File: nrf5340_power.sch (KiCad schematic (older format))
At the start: 0 parts

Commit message: first rev pcb without impedance matching
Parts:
- added C29, C30: 10uF, Capacitor_SMD:C_0201_0603Metric, symbol Device:C_Small
- added D1: LED, LED_SMD:LED_0402_1005Metric, symbol Device:LED
- added D2: MBR120, Diode_SMD:D_SOD-123, symbol Device:D_Zener_Small
- added Q1: Q_PMOS_GSD, Package_TO_SOT_SMD:SOT-23, symbol Device:Q_PMOS_GSD
- added R4, R6: 100k, Resistor_SMD:R_0201_0603Metric, symbol Device:R_Small
- added R5: 68R, Resistor_SMD:R_0201_0603Metric, symbol Device:R_Small
- added U2: AP2112K-3.3, Package_TO_SOT_SMD:SOT-23-5, symbol Regulator_Linear:AP2112K-3.3
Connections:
- new net: C29.1, D2.1 (K), Q1.2 (S), R6.1, U2.1 (VIN)
- new net: R6.2, U2.3 (EN)
- new net: D1.2 (A), R5.2
- new net GND: C29.2, C30.2, D1.1 (K), R4.2, U2.2 (GND)
- new net VBAT: Q1.3 (D)
- new net VBUS: D2.2 (A), Q1.1 (G), R4.1
- new net VDD_nRF: C30.1, R5.1, U2.5 (VOUT)
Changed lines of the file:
@@
 EESchema Schematic File Version 4
-LIBS:nrf5340_module-cache
 EELAYER 30 0
 EELAYER END
 $Descr A4 11693 8268
 encoding utf-8
-Sheet 1 3
+Sheet 3 3
 Title ""
 Date ""
@@
 Comment4 ""
 $EndDescr
+$Comp
+L Device:Q_PMOS_GSD Q1
+U 1 1 5E164004
+P 1450 1050
+F 0 "Q1" H 1655 1096 50  0000 L CNN
+F 1 "Q_PMOS_GSD" H 1655 1005 50  0000 L CNN
+F 2 "Package_TO_SOT_SMD:SOT-23" H 1650 1150 50  0001 C CNN
+F 3 "~" H 1450 1050 50  0001 C CNN
+	1    1450 1050
+	1    0    0    -1
+$EndComp
+$Comp
+L Device:R_Small R4
+U 1 1 5E1648ED
+P 1000 1550
+F 0 "R4" H 750 1600 50  0000 L CNN
+F 1 "100k" H 750 1500 50  0000 L CNN
+F 2 "Resistor_SMD:R_0201_0603Metric" H 1000 1550 50  0001 C CNN
+F 3 "~" H 1000 1550 50  0001 C CNN
+	1    1000 1550
+	1    0    0    -1
+$EndComp
+$Comp
+L Device:D_Zener_Small D2
+U 1 1 5E165282
+P 1300 1400
+F 0 "D2" H 1300 1195 50  0000 C CNN
+F 1 "MBR120" H 1300 1286 50  0000 C CNN
+F 2 "Diode_SMD:D_SOD-123" V 1300 1400 50  0001 C CNN
+F 3 "~" V 1300 1400 50  0001 C CNN
+	1    1300 1400
+	-1   0    0    1
+$EndComp
+$Comp
+L Device:C_Small C29
+U 1 1 5E165C53
+P 1550 1550
+F 0 "C29" H 1642 1596 50  0000 L CNN
+F 1 "10uF" H 1642 1505 50  0000 L CNN
+F 2 "Capacitor_SMD:C_0201_0603Metric" H 1550 1550 50  0001 C CNN
+F 3 "~" H 1550 1550 50  0001 C CNN
+	1    1550 1550
+	1    0    0    -1
+$EndComp
+$Comp
+L Device:C_Small C30
+U 1 1 5E16615D
+P 2800 1550
+F 0 "C30" H 2892 1596 50  0000 L CNN
+F 1 "10uF" H 2892 1505 50  0000 L CNN
+F 2 "Capacitor_SMD:C_0201_0603Metric" H 2800 1550 50  0001 C CNN
+F 3 "~" H 2800 1550 50  0001 C CNN
+	1    2800 1550
+	1    0    0    -1
+$EndComp
+$Comp
+L Device:R_Small R6
+U 1 1 5E1662E7
+P 2000 1500
+F 0 "R6" V 2100 1500 50  0000 C CNN
+F 1 "100k" V 2200 1500 50  0000 C CNN
+F 2 "Resistor_SMD:R_0201_0603Metric" H 2000 1500 50  0001 C CNN
+F 3 "~" H 2000 1500 50  0001 C CNN
+	1    2000 1500
+	0    -1   1    0
+$EndComp
+$Comp
+L Regulator_Linear:AP2112K-3.3 U2
+U 1 1 5E166BA6
+P 2450 1500
+F 0 "U2" H 2450 1842 50  0000 C CNN
+F 1 "AP2112K-3.3" H 2450 1751 50  0000 C CNN
+F 2 "Package_TO_SOT_SMD:SOT-23-5" H 2450 1825 50  0001 C CNN
+F 3 "https://www.diodes.com/assets/Datasheets/AP2112.pdf" H 2450 1600 50  0001 C CNN
+	1    2450 1500
+	1    0    0    -1
+$EndComp
+Text GLabel 2850 1400 2    50   Input ~ 0
+VDD_nRF
+Text GLabel 1000 800  2    50   Input ~ 0
+VBUS
+Text GLabel 1550 800  2    50   Input ~ 0
+VBAT
+Wire Wire Line
+	1550 800  1550 850
+Wire Wire Line
+	1550 1400 1400 1400
+Wire Wire Line
+	1550 1250 1550 1400
+Wire Wire Line
+	1200 1400 1000 1400
+Wire Wire Line
+	1000 1450 1000 1400
+Connection ~ 1000 1400
+Wire Wire Line
+	1000 800  1000 1050
+Wire Wire Line
+	1250 1050 1000 1050
+Connection ~ 1000 1050
+Wire Wire Line
+	1000 1050 1000 1400
+Wire Wire Line
+	1550 1450 1550 1400
+Connection ~ 1550 1400
+Wire Wire Line
+	2100 1500 2150 1500
+Wire Wire Line
+	2150 1400 1850 1400
+Wire Wire Line
+	1850 1400 1850 1500
+Wire Wire Line
+	1850 1500 1900 1500
+Connection ~ 1850 1400
+$Comp
+L power:GND #PWR013
+U 1 1 5E177C45
+P 2800 1700
+F 0 "#PWR013" H 2800 1450 50  0001 C CNN
+F 1 "GND" H 2805 1527 50  0000 C CNN
+F 2 "" H 2800 1700 50  0001 C CNN
+F 3 "" H 2800 1700 50  0001 C CNN
+	1    2800 1700
+	1    0    0    -1
+$EndComp
+$Comp
+L power:GND #PWR012
+U 1 1 5E177E44
+P 2450 1850
+F 0 "#PWR012" H 2450 1600 50  0001 C CNN
+F 1 "GND" H 2455 1677 50  0000 C CNN
+F 2 "" H 2450 1850 50  0001 C CNN
+F 3 "" H 2450 1850 50  0001 C CNN
+	1    2450 1850
+	1    0    0    -1
+$EndComp
+$Comp
+L power:GND #PWR011
+U 1 1 5E17842E
+P 1550 1700
+F 0 "#PWR011" H 1550 1450 50  0001 C CNN
+F 1 "GND" H 1555 1527 50  0000 C CNN
+F 2 "" H 1550 1700 50  0001 C CNN
+F 3 "" H 1550 1700 50  0001 C CNN
+	1    1550 1700
+	1    0    0    -1
+$EndComp
+$Comp
+L power:GND #PWR09
+U 1 1 5E178752
+P 1000 1700
+F 0 "#PWR09" H 1000 1450 50  0001 C CNN
+F 1 "GND" H 1005 1527 50  0000 C CNN
+F 2 "" H 1000 1700 50  0001 C CNN
+F 3 "" H 1000 1700 50  0001 C CNN
+	1    1000 1700
+	1    0    0    -1
+$EndComp
+Wire Wire Line
+	1550 1400 1850 1400
+Wire Wire Line
+	1550 1650 1550 1700
+Wire Wire Line
+	1000 1650 1000 1700
+Wire Wire Line
+	2450 1800 2450 1850
+Wire Wire Line
+	2800 1650 2800 1700
+Wire Wire Line
+	2850 1400 2800 1400
+Wire Wire Line
+	2800 1400 2800 1450
+Connection ~ 2800 1400
+Wire Wire Line
+	2800 1400 2750 1400
+$Comp
+L Device:LED D1
+U 1 1 5E1852C7
+P 1000 2850
+F 0 "D1" V 1039 2733 50  0000 R CNN
+F 1 "LED" V 948 2733 50  0000 R CNN
+F 2 "LED_SMD:LED_0402_1005Metric" H 1000 2850 50  0001 C CNN
+F 3 "~" H 1000 2850 50  0001 C CNN
+	1    1000 2850
+	0    -1   -1   0
+$EndComp
+Text GLabel 1000 2350 2    50   Input ~ 0
+VDD_nRF
+$Comp
+L Device:R_Small R5
+U 1 1 5E18637C
+P 1000 2550
+F 0 "R5" H 850 2600 50  0000 L CNN
+F 1 "68R" H 800 2500 50  0000 L CNN
+F 2 "Resistor_SMD:R_0201_0603Metric" H 1000 2550 50  0001 C CNN
+F 3 "~" H 1000 2550 50  0001 C CNN
+	1    1000 2550
+	1    0    0    -1
+$EndComp
+Wire Wire Line
+	1000 2350 1000 2450
+Wire Wire Line
+	1000 2650 1000 2700
+Wire Wire Line
+	1000 3000 1000 3050
+$Comp
+L power:GND #PWR010
+U 1 1 5E187B31
+P 1000 3050
+F 0 "#PWR010" H 1000 2800 50  0001 C CNN
+F 1 "GND" H 1005 2877 50  0000 C CNN
+F 2 "" H 1000 3050 50  0001 C CNN
+F 3 "" H 1000 3050 50  0001 C CNN
+	1    1000 3050
+	1    0    0    -1
+$EndComp
 $EndSCHEMATC

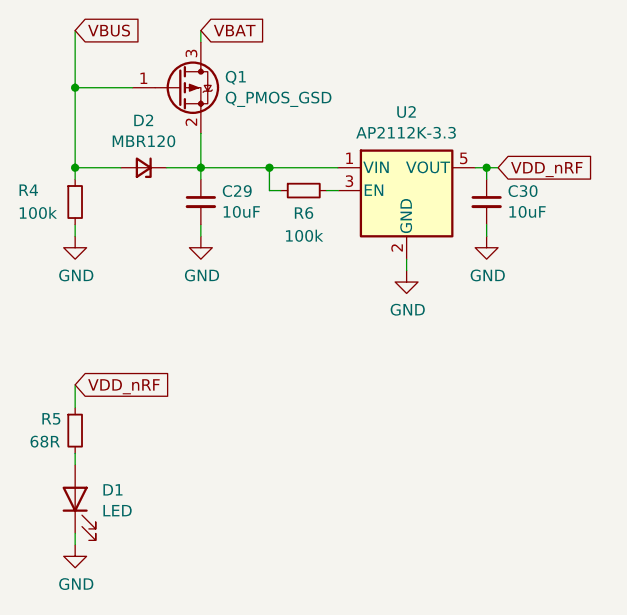
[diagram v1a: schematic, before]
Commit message: fix traces underneath nrf gnd pad and VDD_HV
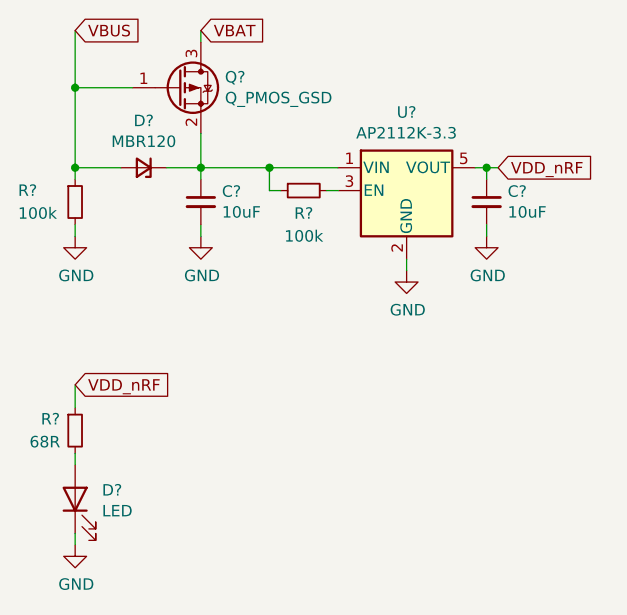
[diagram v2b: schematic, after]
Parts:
- renumbered C29 to C?, C30 to C?, D2 to D?, D1 to D?, Q1 to Q?, R4 to R?, R6 to R?, R5 to R?, U2 to U?
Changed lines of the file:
@@
 EESchema Schematic File Version 4
+LIBS:nrf5340_module-cache
 EELAYER 30 0
 EELAYER END
@@
 $EndDescr
 $Comp
-L Device:Q_PMOS_GSD Q1
+L Device:Q_PMOS_GSD Q?
 U 1 1 5E164004
 P 1450 1050
-F 0 "Q1" H 1655 1096 50  0000 L CNN
+F 0 "Q?" H 1655 1096 50  0000 L CNN
 F 1 "Q_PMOS_GSD" H 1655 1005 50  0000 L CNN
 F 2 "Package_TO_SOT_SMD:SOT-23" H 1650 1150 50  0001 C CNN
@@
 $EndComp
 $Comp
-L Device:R_Small R4
+L Device:R_Small R?
 U 1 1 5E1648ED
 P 1000 1550
-F 0 "R4" H 750 1600 50  0000 L CNN
+F 0 "R?" H 750 1600 50  0000 L CNN
 F 1 "100k" H 750 1500 50  0000 L CNN
 F 2 "Resistor_SMD:R_0201_0603Metric" H 1000 1550 50  0001 C CNN
@@
 $EndComp
 $Comp
-L Device:D_Zener_Small D2
+L Device:D_Zener_Small D?
 U 1 1 5E165282
 P 1300 1400
-F 0 "D2" H 1300 1195 50  0000 C CNN
+F 0 "D?" H 1300 1195 50  0000 C CNN
 F 1 "MBR120" H 1300 1286 50  0000 C CNN
 F 2 "Diode_SMD:D_SOD-123" V 1300 1400 50  0001 C CNN
@@
 $EndComp
 $Comp
-L Device:C_Small C29
+L Device:C_Small C?
 U 1 1 5E165C53
 P 1550 1550
-F 0 "C29" H 1642 1596 50  0000 L CNN
+F 0 "C?" H 1642 1596 50  0000 L CNN
 F 1 "10uF" H 1642 1505 50  0000 L CNN
 F 2 "Capacitor_SMD:C_0201_0603Metric" H 1550 1550 50  0001 C CNN
@@
 $EndComp
 $Comp
-L Device:C_Small C30
+L Device:C_Small C?
 U 1 1 5E16615D
 P 2800 1550
-F 0 "C30" H 2892 1596 50  0000 L CNN
+F 0 "C?" H 2892 1596 50  0000 L CNN
 F 1 "10uF" H 2892 1505 50  0000 L CNN
 F 2 "Capacitor_SMD:C_0201_0603Metric" H 2800 1550 50  0001 C CNN
@@
 $EndComp
 $Comp
-L Device:R_Small R6
+L Device:R_Small R?
 U 1 1 5E1662E7
 P 2000 1500
-F 0 "R6" V 2100 1500 50  0000 C CNN
+F 0 "R?" V 2100 1500 50  0000 C CNN
 F 1 "100k" V 2200 1500 50  0000 C CNN
 F 2 "Resistor_SMD:R_0201_0603Metric" H 2000 1500 50  0001 C CNN
@@
 $EndComp
 $Comp
-L Regulator_Linear:AP2112K-3.3 U2
+L Regulator_Linear:AP2112K-3.3 U?
 U 1 1 5E166BA6
 P 2450 1500
-F 0 "U2" H 2450 1842 50  0000 C CNN
+F 0 "U?" H 2450 1842 50  0000 C CNN
 F 1 "AP2112K-3.3" H 2450 1751 50  0000 C CNN
 F 2 "Package_TO_SOT_SMD:SOT-23-5" H 2450 1825 50  0001 C CNN
@@
 Connection ~ 1850 1400
 $Comp
-L power:GND #PWR013
+L power:GND #PWR?
 U 1 1 5E177C45
 P 2800 1700
-F 0 "#PWR013" H 2800 1450 50  0001 C CNN
+F 0 "#PWR?" H 2800 1450 50  0001 C CNN
 F 1 "GND" H 2805 1527 50  0000 C CNN
 F 2 "" H 2800 1700 50  0001 C CNN
@@
 $EndComp
 $Comp
-L power:GND #PWR012
+L power:GND #PWR?
 U 1 1 5E177E44
 P 2450 1850
-F 0 "#PWR012" H 2450 1600 50  0001 C CNN
+F 0 "#PWR?" H 2450 1600 50  0001 C CNN
 F 1 "GND" H 2455 1677 50  0000 C CNN
 F 2 "" H 2450 1850 50  0001 C CNN
@@
 $EndComp
 $Comp
-L power:GND #PWR011
+L power:GND #PWR?
 U 1 1 5E17842E
 P 1550 1700
-F 0 "#PWR011" H 1550 1450 50  0001 C CNN
+F 0 "#PWR?" H 1550 1450 50  0001 C CNN
 F 1 "GND" H 1555 1527 50  0000 C CNN
 F 2 "" H 1550 1700 50  0001 C CNN
@@
 $EndComp
 $Comp
-L power:GND #PWR09
+L power:GND #PWR?
 U 1 1 5E178752
 P 1000 1700
-F 0 "#PWR09" H 1000 1450 50  0001 C CNN
+F 0 "#PWR?" H 1000 1450 50  0001 C CNN
 F 1 "GND" H 1005 1527 50  0000 C CNN
 F 2 "" H 1000 1700 50  0001 C CNN
@@
 	2800 1400 2750 1400
 $Comp
-L Device:LED D1
+L Device:LED D?
 U 1 1 5E1852C7
 P 1000 2850
-F 0 "D1" V 1039 2733 50  0000 R CNN
+F 0 "D?" V 1039 2733 50  0000 R CNN
 F 1 "LED" V 948 2733 50  0000 R CNN
 F 2 "LED_SMD:LED_0402_1005Metric" H 1000 2850 50  0001 C CNN
@@
 VDD_nRF
 $Comp
-L Device:R_Small R5
+L Device:R_Small R?
 U 1 1 5E18637C
 P 1000 2550
-F 0 "R5" H 850 2600 50  0000 L CNN
+F 0 "R?" H 850 2600 50  0000 L CNN
 F 1 "68R" H 800 2500 50  0000 L CNN
 F 2 "Resistor_SMD:R_0201_0603Metric" H 1000 2550 50  0001 C CNN
@@
 	1000 3000 1000 3050
 $Comp
-L power:GND #PWR010
+L power:GND #PWR?
 U 1 1 5E187B31
 P 1000 3050
-F 0 "#PWR010" H 1000 2800 50  0001 C CNN
+F 0 "#PWR?" H 1000 2800 50  0001 C CNN
 F 1 "GND" H 1005 2877 50  0000 C CNN
 F 2 "" H 1000 3050 50  0001 C CNN

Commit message: fix vdd_hv
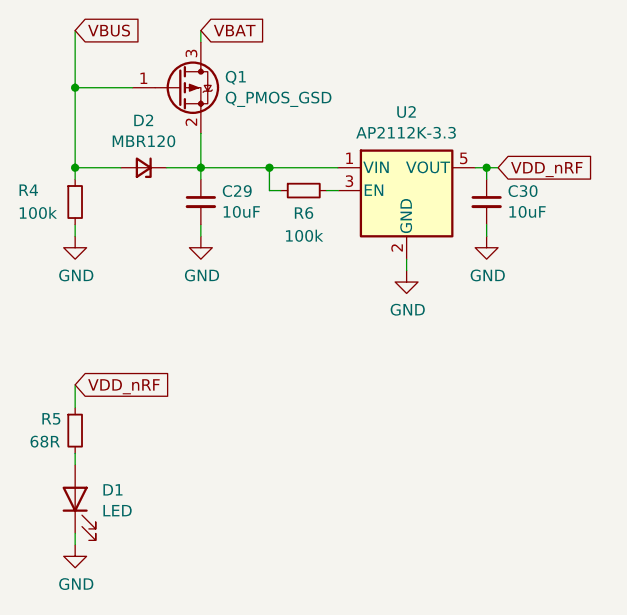
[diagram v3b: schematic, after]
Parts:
- gave numbers to parts that had none: 9
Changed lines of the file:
@@
 $EndDescr
 $Comp
-L Device:Q_PMOS_GSD Q?
+L Device:Q_PMOS_GSD Q1
 U 1 1 5E164004
 P 1450 1050
-F 0 "Q?" H 1655 1096 50  0000 L CNN
+F 0 "Q1" H 1655 1096 50  0000 L CNN
 F 1 "Q_PMOS_GSD" H 1655 1005 50  0000 L CNN
 F 2 "Package_TO_SOT_SMD:SOT-23" H 1650 1150 50  0001 C CNN
@@
 $EndComp
 $Comp
-L Device:R_Small R?
+L Device:R_Small R4
 U 1 1 5E1648ED
 P 1000 1550
-F 0 "R?" H 750 1600 50  0000 L CNN
+F 0 "R4" H 750 1600 50  0000 L CNN
 F 1 "100k" H 750 1500 50  0000 L CNN
 F 2 "Resistor_SMD:R_0201_0603Metric" H 1000 1550 50  0001 C CNN
@@
 $EndComp
 $Comp
-L Device:D_Zener_Small D?
+L Device:D_Zener_Small D2
 U 1 1 5E165282
 P 1300 1400
-F 0 "D?" H 1300 1195 50  0000 C CNN
+F 0 "D2" H 1300 1195 50  0000 C CNN
 F 1 "MBR120" H 1300 1286 50  0000 C CNN
 F 2 "Diode_SMD:D_SOD-123" V 1300 1400 50  0001 C CNN
@@
 $EndComp
 $Comp
-L Device:C_Small C?
+L Device:C_Small C29
 U 1 1 5E165C53
 P 1550 1550
-F 0 "C?" H 1642 1596 50  0000 L CNN
+F 0 "C29" H 1642 1596 50  0000 L CNN
 F 1 "10uF" H 1642 1505 50  0000 L CNN
 F 2 "Capacitor_SMD:C_0201_0603Metric" H 1550 1550 50  0001 C CNN
@@
 $EndComp
 $Comp
-L Device:C_Small C?
+L Device:C_Small C30
 U 1 1 5E16615D
 P 2800 1550
-F 0 "C?" H 2892 1596 50  0000 L CNN
+F 0 "C30" H 2892 1596 50  0000 L CNN
 F 1 "10uF" H 2892 1505 50  0000 L CNN
 F 2 "Capacitor_SMD:C_0201_0603Metric" H 2800 1550 50  0001 C CNN
@@
 $EndComp
 $Comp
-L Device:R_Small R?
+L Device:R_Small R6
 U 1 1 5E1662E7
 P 2000 1500
-F 0 "R?" V 2100 1500 50  0000 C CNN
+F 0 "R6" V 2100 1500 50  0000 C CNN
 F 1 "100k" V 2200 1500 50  0000 C CNN
 F 2 "Resistor_SMD:R_0201_0603Metric" H 2000 1500 50  0001 C CNN
@@
 $EndComp
 $Comp
-L Regulator_Linear:AP2112K-3.3 U?
+L Regulator_Linear:AP2112K-3.3 U2
 U 1 1 5E166BA6
 P 2450 1500
-F 0 "U?" H 2450 1842 50  0000 C CNN
+F 0 "U2" H 2450 1842 50  0000 C CNN
 F 1 "AP2112K-3.3" H 2450 1751 50  0000 C CNN
 F 2 "Package_TO_SOT_SMD:SOT-23-5" H 2450 1825 50  0001 C CNN
@@
 Connection ~ 1850 1400
 $Comp
-L power:GND #PWR?
+L power:GND #PWR0130
 U 1 1 5E177C45
 P 2800 1700
-F 0 "#PWR?" H 2800 1450 50  0001 C CNN
+F 0 "#PWR0130" H 2800 1450 50  0001 C CNN
 F 1 "GND" H 2805 1527 50  0000 C CNN
 F 2 "" H 2800 1700 50  0001 C CNN
@@
 $EndComp
 $Comp
-L power:GND #PWR?
+L power:GND #PWR0131
 U 1 1 5E177E44
 P 2450 1850
-F 0 "#PWR?" H 2450 1600 50  0001 C CNN
+F 0 "#PWR0131" H 2450 1600 50  0001 C CNN
 F 1 "GND" H 2455 1677 50  0000 C CNN
 F 2 "" H 2450 1850 50  0001 C CNN
@@
 $EndComp
 $Comp
-L power:GND #PWR?
+L power:GND #PWR0132
 U 1 1 5E17842E
 P 1550 1700
-F 0 "#PWR?" H 1550 1450 50  0001 C CNN
+F 0 "#PWR0132" H 1550 1450 50  0001 C CNN
 F 1 "GND" H 1555 1527 50  0000 C CNN
 F 2 "" H 1550 1700 50  0001 C CNN
@@
 $EndComp
 $Comp
-L power:GND #PWR?
+L power:GND #PWR0133
 U 1 1 5E178752
 P 1000 1700
-F 0 "#PWR?" H 1000 1450 50  0001 C CNN
+F 0 "#PWR0133" H 1000 1450 50  0001 C CNN
 F 1 "GND" H 1005 1527 50  0000 C CNN
 F 2 "" H 1000 1700 50  0001 C CNN
@@
 	2800 1400 2750 1400
 $Comp
-L Device:LED D?
+L Device:LED D1
 U 1 1 5E1852C7
 P 1000 2850
-F 0 "D?" V 1039 2733 50  0000 R CNN
+F 0 "D1" V 1039 2733 50  0000 R CNN
 F 1 "LED" V 948 2733 50  0000 R CNN
 F 2 "LED_SMD:LED_0402_1005Metric" H 1000 2850 50  0001 C CNN
@@
 VDD_nRF
 $Comp
-L Device:R_Small R?
+L Device:R_Small R5
 U 1 1 5E18637C
 P 1000 2550
-F 0 "R?" H 850 2600 50  0000 L CNN
+F 0 "R5" H 850 2600 50  0000 L CNN
 F 1 "68R" H 800 2500 50  0000 L CNN
 F 2 "Resistor_SMD:R_0201_0603Metric" H 1000 2550 50  0001 C CNN
@@
 	1000 3000 1000 3050
 $Comp
-L power:GND #PWR?
+L power:GND #PWR0134
 U 1 1 5E187B31
 P 1000 3050
-F 0 "#PWR?" H 1000 2800 50  0001 C CNN
+F 0 "#PWR0134" H 1000 2800 50  0001 C CNN
 F 1 "GND" H 1005 2877 50  0000 C CNN
 F 2 "" H 1000 3050 50  0001 C CNN

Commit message: fix vddh stuff
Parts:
- renumbered C29 to C?, C30 to C?, D2 to D?, D1 to D?, Q1 to Q?, R4 to R?, R6 to R?, R5 to R?, U2 to U?
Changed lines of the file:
@@
 $Descr A4 11693 8268
 encoding utf-8
-Sheet 3 3
+Sheet 3 7
 Title ""
 Date ""
@@
 $EndDescr
 $Comp
-L Device:Q_PMOS_GSD Q1
+L Device:Q_PMOS_GSD Q?
 U 1 1 5E164004
 P 1450 1050
-F 0 "Q1" H 1655 1096 50  0000 L CNN
+F 0 "Q?" H 1655 1096 50  0000 L CNN
 F 1 "Q_PMOS_GSD" H 1655 1005 50  0000 L CNN
 F 2 "Package_TO_SOT_SMD:SOT-23" H 1650 1150 50  0001 C CNN
@@
 $EndComp
 $Comp
-L Device:R_Small R4
+L Device:R_Small R?
 U 1 1 5E1648ED
 P 1000 1550
-F 0 "R4" H 750 1600 50  0000 L CNN
+F 0 "R?" H 750 1600 50  0000 L CNN
 F 1 "100k" H 750 1500 50  0000 L CNN
 F 2 "Resistor_SMD:R_0201_0603Metric" H 1000 1550 50  0001 C CNN
@@
 $EndComp
 $Comp
-L Device:D_Zener_Small D2
+L Device:D_Zener_Small D?
 U 1 1 5E165282
 P 1300 1400
-F 0 "D2" H 1300 1195 50  0000 C CNN
+F 0 "D?" H 1300 1195 50  0000 C CNN
 F 1 "MBR120" H 1300 1286 50  0000 C CNN
 F 2 "Diode_SMD:D_SOD-123" V 1300 1400 50  0001 C CNN
@@
 $EndComp
 $Comp
-L Device:C_Small C29
+L Device:C_Small C?
 U 1 1 5E165C53
 P 1550 1550
-F 0 "C29" H 1642 1596 50  0000 L CNN
+F 0 "C?" H 1642 1596 50  0000 L CNN
 F 1 "10uF" H 1642 1505 50  0000 L CNN
 F 2 "Capacitor_SMD:C_0201_0603Metric" H 1550 1550 50  0001 C CNN
@@
 $EndComp
 $Comp
-L Device:C_Small C30
+L Device:C_Small C?
 U 1 1 5E16615D
 P 2800 1550
-F 0 "C30" H 2892 1596 50  0000 L CNN
+F 0 "C?" H 2892 1596 50  0000 L CNN
 F 1 "10uF" H 2892 1505 50  0000 L CNN
 F 2 "Capacitor_SMD:C_0201_0603Metric" H 2800 1550 50  0001 C CNN
@@
 $EndComp
 $Comp
-L Device:R_Small R6
+L Device:R_Small R?
 U 1 1 5E1662E7
 P 2000 1500
-F 0 "R6" V 2100 1500 50  0000 C CNN
+F 0 "R?" V 2100 1500 50  0000 C CNN
 F 1 "100k" V 2200 1500 50  0000 C CNN
 F 2 "Resistor_SMD:R_0201_0603Metric" H 2000 1500 50  0001 C CNN
@@
 $EndComp
 $Comp
-L Regulator_Linear:AP2112K-3.3 U2
+L Regulator_Linear:AP2112K-3.3 U?
 U 1 1 5E166BA6
 P 2450 1500
-F 0 "U2" H 2450 1842 50  0000 C CNN
+F 0 "U?" H 2450 1842 50  0000 C CNN
 F 1 "AP2112K-3.3" H 2450 1751 50  0000 C CNN
 F 2 "Package_TO_SOT_SMD:SOT-23-5" H 2450 1825 50  0001 C CNN
@@
 Connection ~ 1850 1400
 $Comp
-L power:GND #PWR0130
+L power:GND #PWR?
 U 1 1 5E177C45
 P 2800 1700
-F 0 "#PWR0130" H 2800 1450 50  0001 C CNN
+F 0 "#PWR?" H 2800 1450 50  0001 C CNN
 F 1 "GND" H 2805 1527 50  0000 C CNN
 F 2 "" H 2800 1700 50  0001 C CNN
@@
 $EndComp
 $Comp
-L power:GND #PWR0131
+L power:GND #PWR?
 U 1 1 5E177E44
 P 2450 1850
-F 0 "#PWR0131" H 2450 1600 50  0001 C CNN
+F 0 "#PWR?" H 2450 1600 50  0001 C CNN
 F 1 "GND" H 2455 1677 50  0000 C CNN
 F 2 "" H 2450 1850 50  0001 C CNN
@@
 $EndComp
 $Comp
-L power:GND #PWR0132
+L power:GND #PWR?
 U 1 1 5E17842E
 P 1550 1700
-F 0 "#PWR0132" H 1550 1450 50  0001 C CNN
+F 0 "#PWR?" H 1550 1450 50  0001 C CNN
 F 1 "GND" H 1555 1527 50  0000 C CNN
 F 2 "" H 1550 1700 50  0001 C CNN
@@
 $EndComp
 $Comp
-L power:GND #PWR0133
+L power:GND #PWR?
 U 1 1 5E178752
 P 1000 1700
-F 0 "#PWR0133" H 1000 1450 50  0001 C CNN
+F 0 "#PWR?" H 1000 1450 50  0001 C CNN
 F 1 "GND" H 1005 1527 50  0000 C CNN
 F 2 "" H 1000 1700 50  0001 C CNN
@@
 	2800 1400 2750 1400
 $Comp
-L Device:LED D1
+L Device:LED D?
 U 1 1 5E1852C7
 P 1000 2850
-F 0 "D1" V 1039 2733 50  0000 R CNN
+F 0 "D?" V 1039 2733 50  0000 R CNN
 F 1 "LED" V 948 2733 50  0000 R CNN
 F 2 "LED_SMD:LED_0402_1005Metric" H 1000 2850 50  0001 C CNN
@@
 VDD_nRF
 $Comp
-L Device:R_Small R5
+L Device:R_Small R?
 U 1 1 5E18637C
 P 1000 2550
-F 0 "R5" H 850 2600 50  0000 L CNN
+F 0 "R?" H 850 2600 50  0000 L CNN
 F 1 "68R" H 800 2500 50  0000 L CNN
 F 2 "Resistor_SMD:R_0201_0603Metric" H 1000 2550 50  0001 C CNN
@@
 	1000 3000 1000 3050
 $Comp
-L power:GND #PWR0134
+L power:GND #PWR?
 U 1 1 5E187B31
 P 1000 3050
-F 0 "#PWR0134" H 1000 2800 50  0001 C CNN
+F 0 "#PWR?" H 1000 2800 50  0001 C CNN
 F 1 "GND" H 1005 2877 50  0000 C CNN
 F 2 "" H 1000 3050 50  0001 C CNN
